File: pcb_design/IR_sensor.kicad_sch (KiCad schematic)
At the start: 36 parts, among them J6 IR_1, J7 IR_3, J8 IR_2, J9 IR_4, Q2 DMN3065LW-7, Q3 DMN3065LW-7, Q4 DMN3065LW-7, Q5 DMN3065LW-7

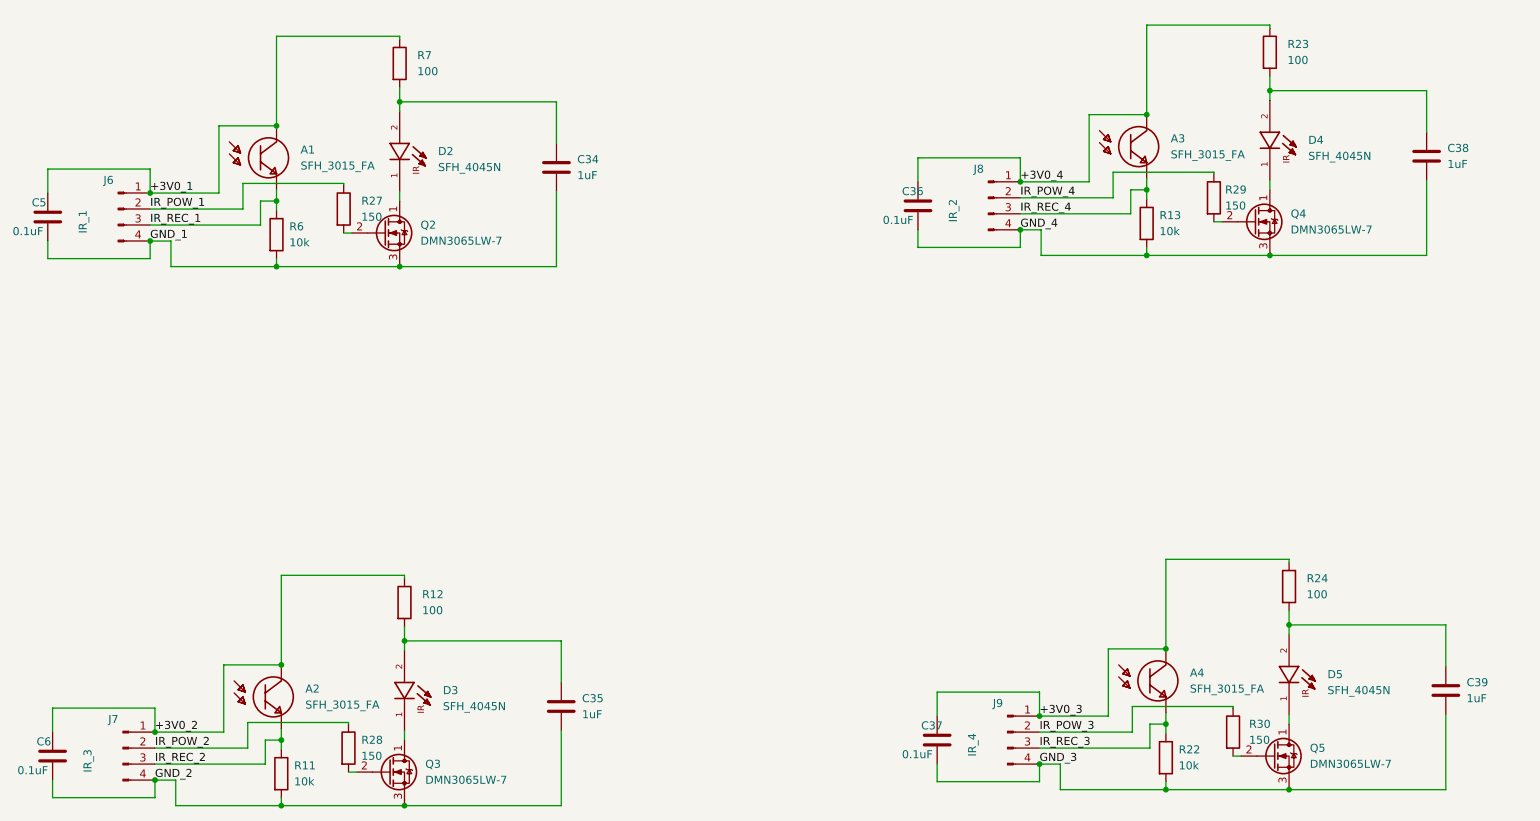
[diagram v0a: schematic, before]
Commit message: Update mushak PCB with new changes * Add AMS1117 as 3.3v regulator * Add new alternate placement for IR sensors * Add new 3.3v compatible ToF sensor * Update gerber files
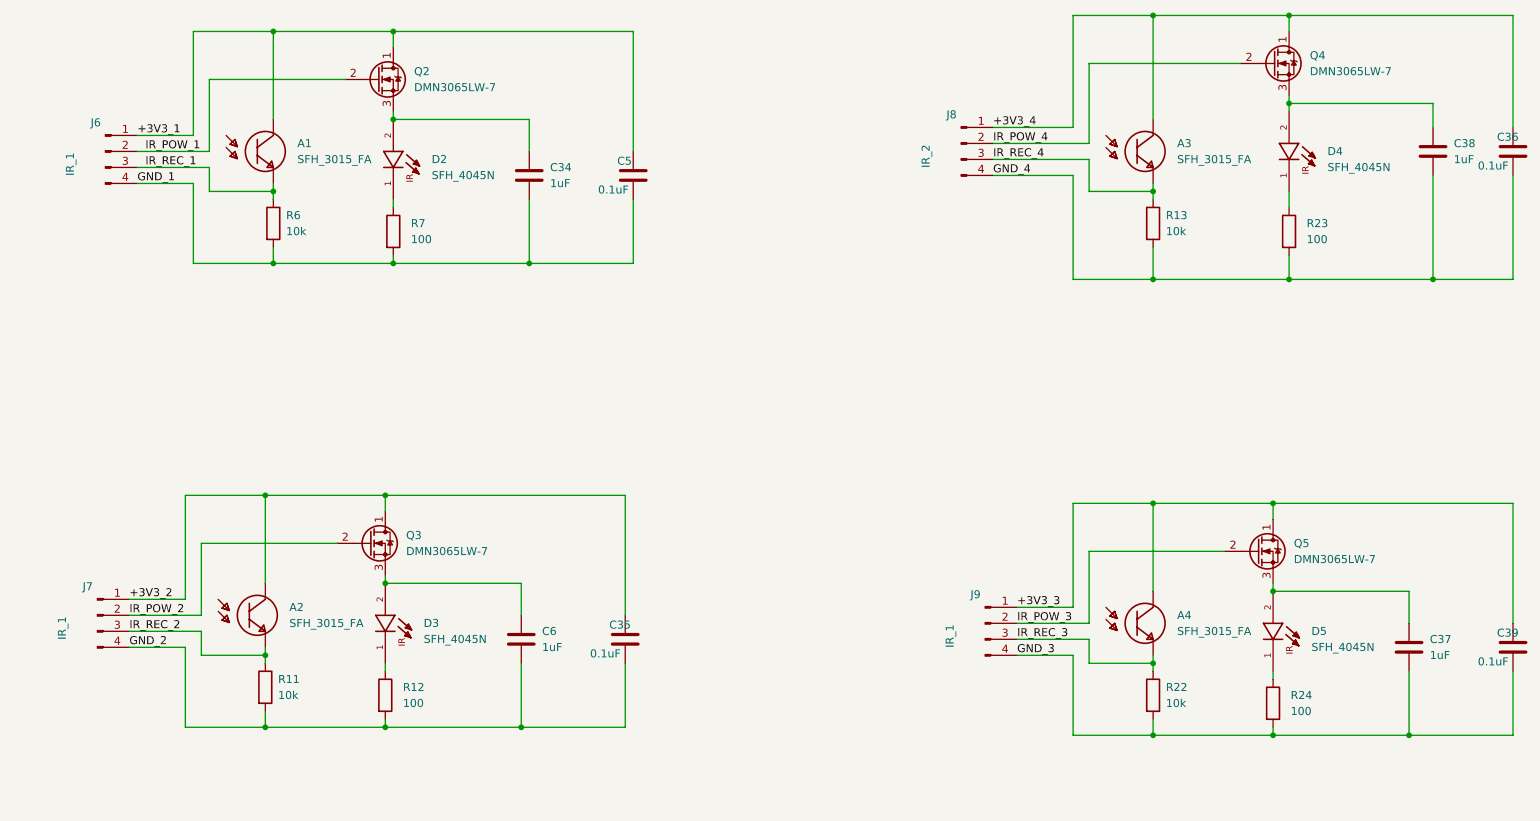
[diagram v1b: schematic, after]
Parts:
- removed R27, R28, R29, R30: 150, Resistor_SMD:R_0402_1005Metric, symbol Device:R
- C35, C39: value 1uF -> 0.1uF; footprint Capacitor_SMD:C_0603_1608Metric -> Capacitor_SMD:C_0402_1005Metric
- C37, C6: value 0.1uF -> 1uF; footprint Capacitor_SMD:C_0402_1005Metric -> Capacitor_SMD:C_0603_1608Metric
- J7: value IR_3 -> IR_1
- J9: value IR_4 -> IR_1
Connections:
- net GND_1: now also R7.2; no longer Q2.3 (S)
- net GND_2: now also R12.2; no longer Q3.3 (S)
- net GND_3: now also R24.2; no longer Q5.3 (S)
- net GND_4: now also R23.2; no longer Q4.3 (S)
- net IR_POW_1: now also Q2.2 (G)
- net IR_POW_2: now also Q3.2 (G)
- net IR_POW_3: now also Q5.2 (G)
- net IR_POW_4: now also Q4.2 (G)
- net at D4.1: now also R23.1; no longer Q4.1 (D)
- net at C38.1, D4.2: now also Q4.3 (S); no longer R23.2
- net at D3.1: now also R12.1; no longer Q3.1 (D)
- net at C34.1, D2.2: now also Q2.3 (S); no longer R7.2
- net at D2.1: now also R7.1; no longer Q2.1 (D)
- net at D5.1: now also R24.1; no longer Q5.1 (D)
- net +3V0_1 renamed +3V3_1
- net +3V3_1: now also Q2.1 (D); no longer R7.1
- net +3V0_2 renamed +3V3_2
- net +3V3_2: now also C35.1, Q3.1 (D); no longer C6.1, R12.1
- net +3V0_3 renamed +3V3_3
- net +3V3_3: now also C39.1, Q5.1 (D); no longer C37.1, R24.1
- net +3V0_4 renamed +3V3_4
- net +3V3_4: now also Q4.1 (D); no longer R23.1
- new net: C6.1, D3.2, Q3.3 (S)
- new net: C37.1, D5.2, Q5.3 (S)
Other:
- moved on the sheet: A1, A3, C34, C36, C38, C5, D2, D4, J6, J8, Q2, Q4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
